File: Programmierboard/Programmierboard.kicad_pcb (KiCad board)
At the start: 2 copper layers, 179 x 99 mm, 37 parts, among them J1 Conn_01x10_Socket, J2 Conn_01x10_Socket, J3 Conn_01x10_Socket, J4 Conn_01x10_Socket, J5 DE9_Plug_MountingHoles, J6 Conn_01x10_Socket, J7 Conn_01x10_Socket, Q1 BC327, Q2 BC327, SW1 SW_SPDT, U1 AT89C2051-12P, U2 MAX202, U99 L7805

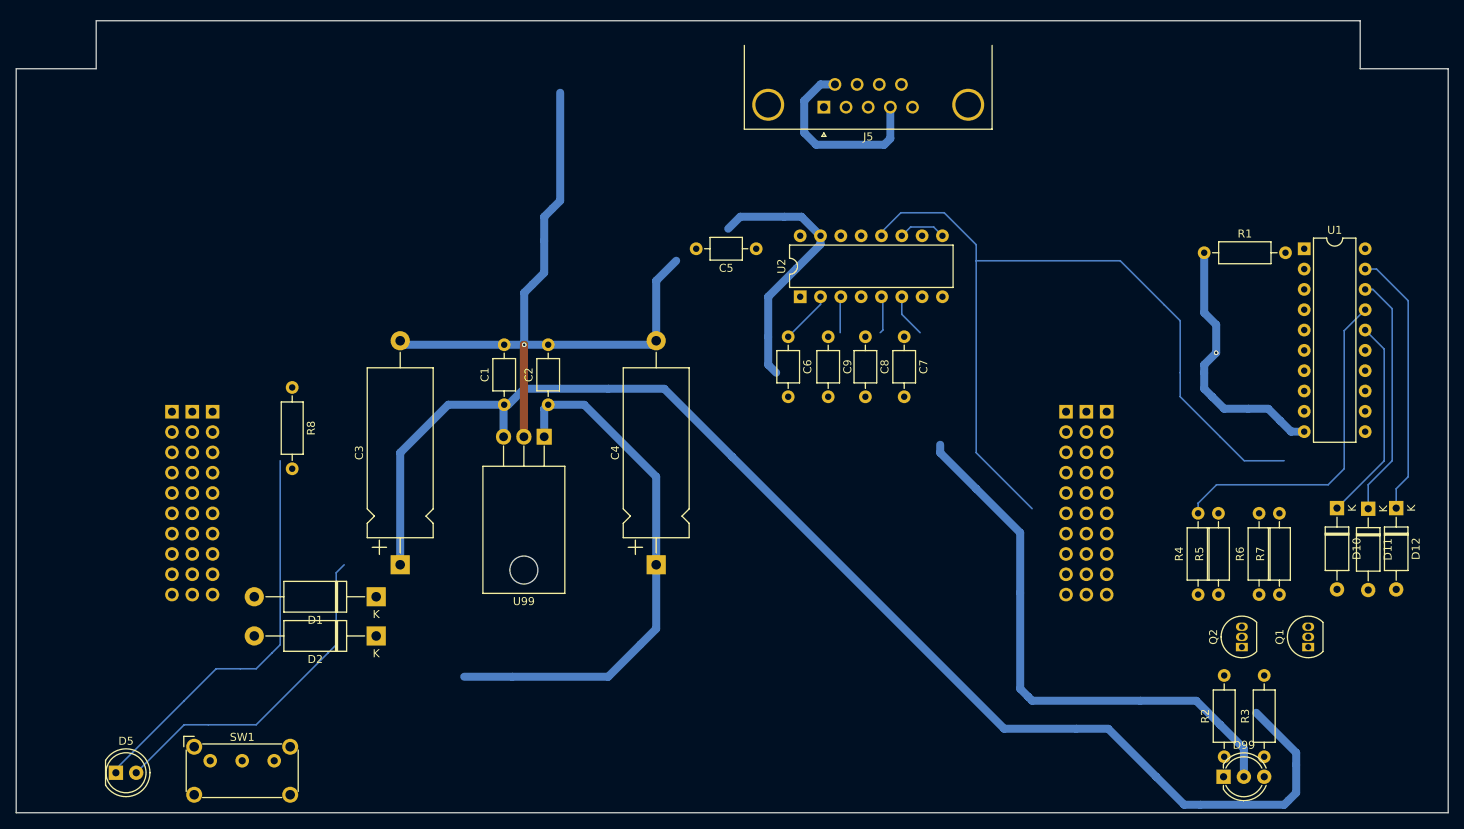
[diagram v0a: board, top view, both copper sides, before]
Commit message: footprints und symbole
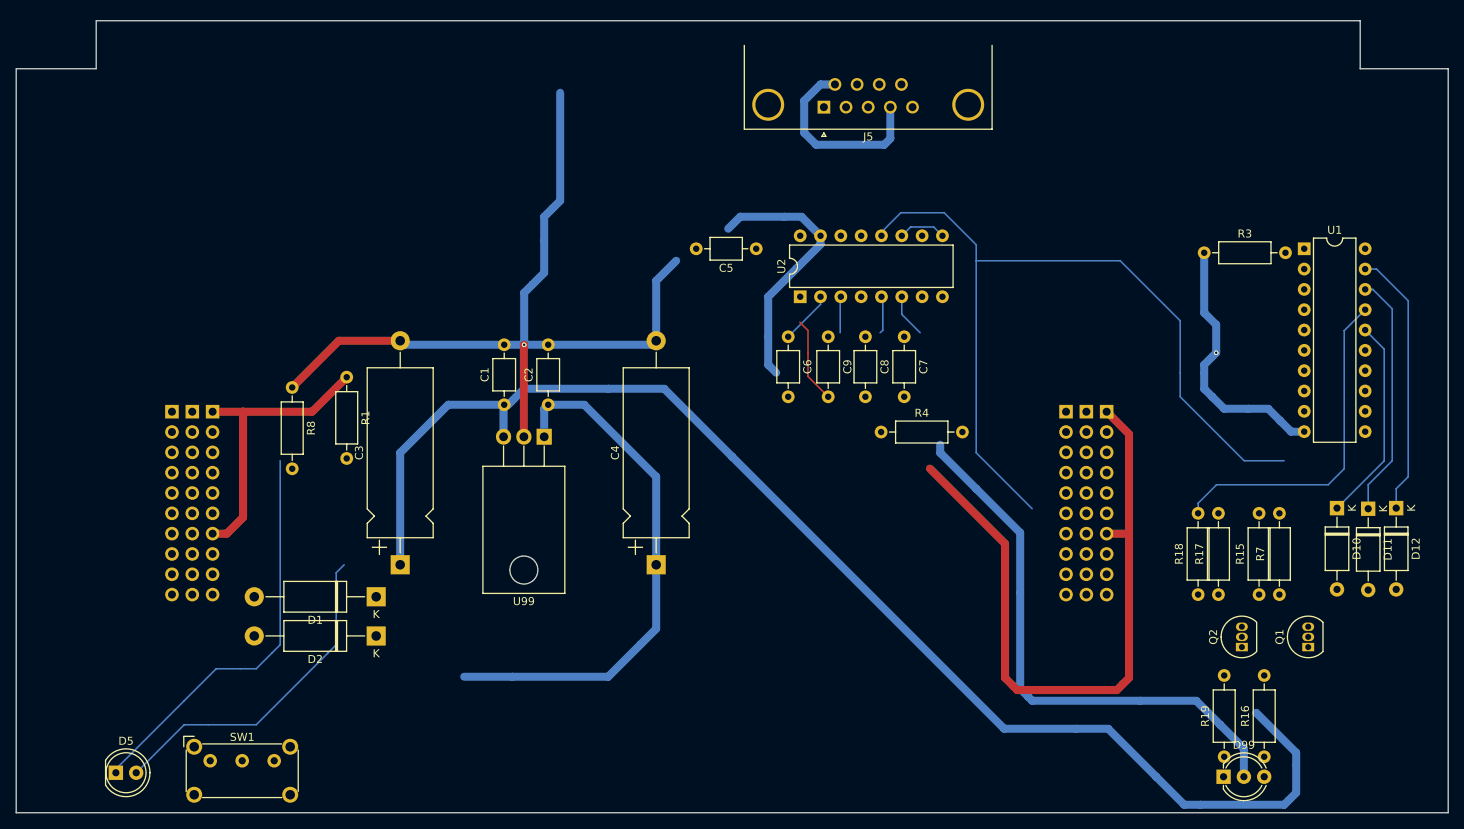
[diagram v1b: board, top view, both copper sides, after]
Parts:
- added R1: R, Resistor_THT:R_Axial_DIN0207_L6.3mm_D2.5mm_P10.16mm_Horizontal, F.Cu at (99.3, 98.6)
- added R4: R, Resistor_THT:R_Axial_DIN0207_L6.3mm_D2.5mm_P10.16mm_Horizontal, F.Cu at (166.1, 105.4)
- renumbered R6 to R15, R3 to R16, R5 to R17, R4 to R18, R2 to R19, R1 to R3
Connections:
- J1 pad 1: unconnected-(J1-Pin_1-Pad1) -> Net-(J1-Pin_1)
- J1 pad 7: unconnected-(J1-Pin_7-Pad7) -> Net-(J1-Pin_1)
- J4 pad 1: unconnected-(J4-Pin_1-Pad1) -> Net-(J4-Pin_1)
- J4 pad 7: unconnected-(J4-Pin_7-Pad7) -> Net-(J4-Pin_1)
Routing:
- net Net-(J1-Pin_1): track 0.00 -> 84.0 mm
- net Net-(J4-Pin_1): track 0.00 -> 36.4 mm
- net GND: track 223.9 -> 239.8 mm
- net unconnected-(C9-Pad2): track 0.00 -> 10.8 mm

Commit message: prog
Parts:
- added C10: C, Capacitor_THT:C_Axial_L3.8mm_D2.6mm_P7.50mm_Horizontal, F.Cu at (221.4, 79.4)
- added J8: Conn_01x02_Socket, Connector_PinSocket_2.54mm:PinSocket_1x02_P2.54mm_Vertical, F.Cu at (119.5, 82.5)
- D5: value LED -> POWER
- moved Q2 4.89 mm to (206.4, 131.6)
- moved Q1 4.78 mm to (214.8, 131.7)
- moved R19 3.58 mm to (205.7, 144.5)
- moved R16 3.34 mm to (211.1, 144.4)
- moved D99 2.94 mm to (206.0, 148.2)
- moved U2 1.87 mm to (154.3, 89.3)
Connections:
- C1 pad 1: Net-(U99-OUT) -> VCC
- C3 pad 1: Net-(U99-OUT) -> VCC
- C5 pad 1: unconnected-(C5-Pad1) -> Net-(J1-Pin_1)
- C6 pad 2: unconnected-(C6-Pad2) -> GND
- C7 pad 2: unconnected-(C7-Pad2) -> GND
- D5 pad 2: unconnected-(D5-A-Pad2) -> VCC
- J4 pad 1: Net-(J4-Pin_1) -> Net-(J1-Pin_1)
- J4 pad 7: Net-(J4-Pin_1) -> Net-(J1-Pin_1)
- R1 pad 1: Net-(J4-Pin_1) -> Net-(J1-Pin_1)
- R1 pad 2: unconnected-(R1-Pad2) -> VCC
- R15 pad 2: Net-(R15-Pad2) -> VCC
- R17 pad 2: Net-(R15-Pad2) -> VCC
- U1 pad 20: unconnected-(U1-VCC-Pad20) -> VCC
- U99 pad 3: Net-(U99-OUT) -> VCC
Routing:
- net VCC: track 0.00 -> 251.6 mm
- net GND: track 239.8 -> 418.7 mm
- net Net-(U99-OUT): track 167.6 -> 0.00 mm
- net Net-(J1-Pin_1): track 84.0 -> 217.4 mm
- net +12V: track 0.00 -> 81.3 mm
- net unconnected-(D5-A-Pad2): track 42.0 -> 0.00 mm
- net Net-(J4-Pin_1): track 36.4 -> 0.00 mm
- net Net-(D1-K): track 66.9 -> 82.1 mm
- net unconnected-(U2-R1OUT-Pad12): track 105.3 -> 107.0 mm
- net Net-(U2-VS+): track 5.97 -> 4.48 mm

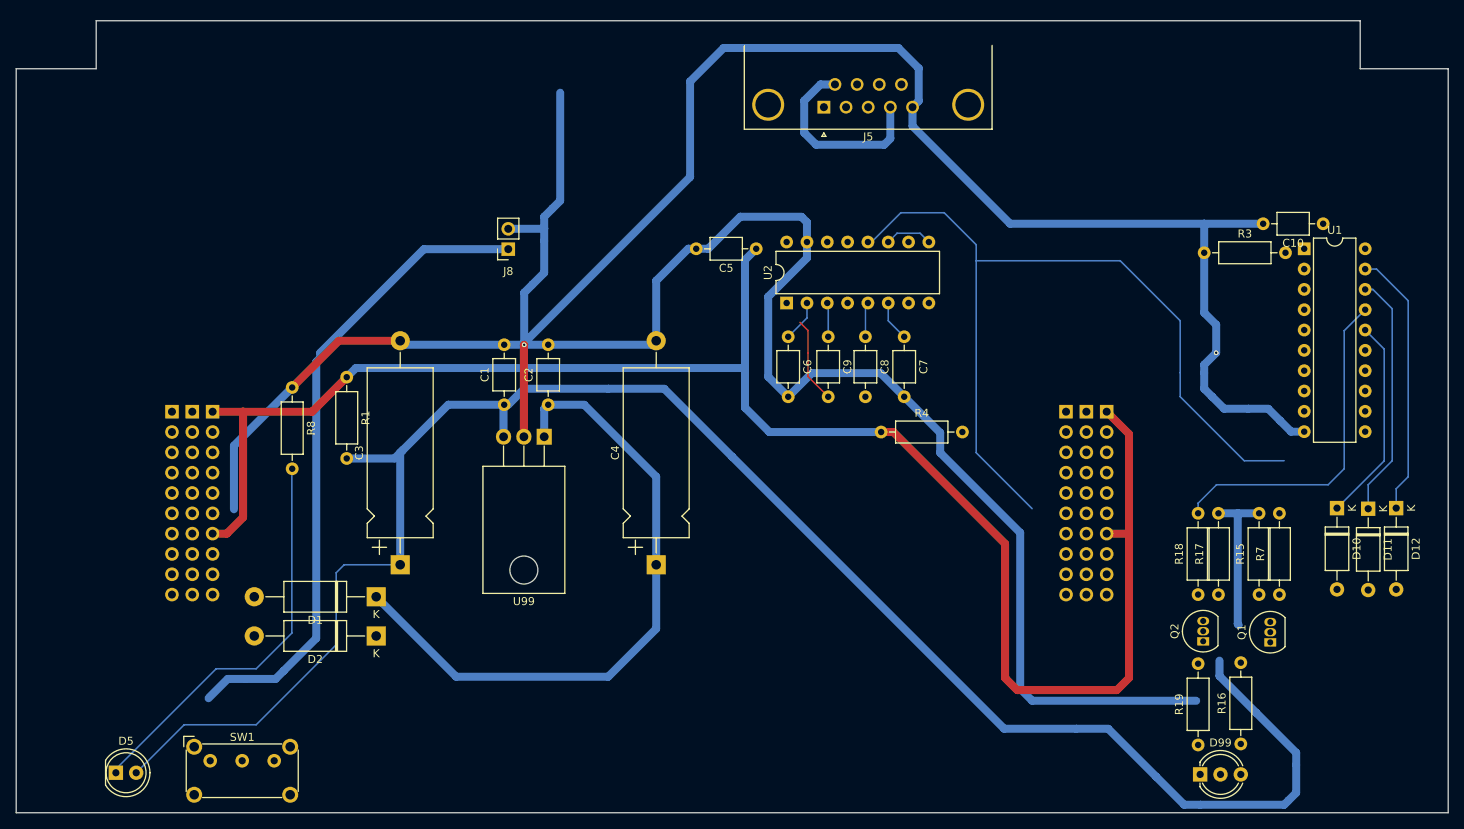
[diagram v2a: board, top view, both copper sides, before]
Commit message: programmierboard bis auf 2 linien
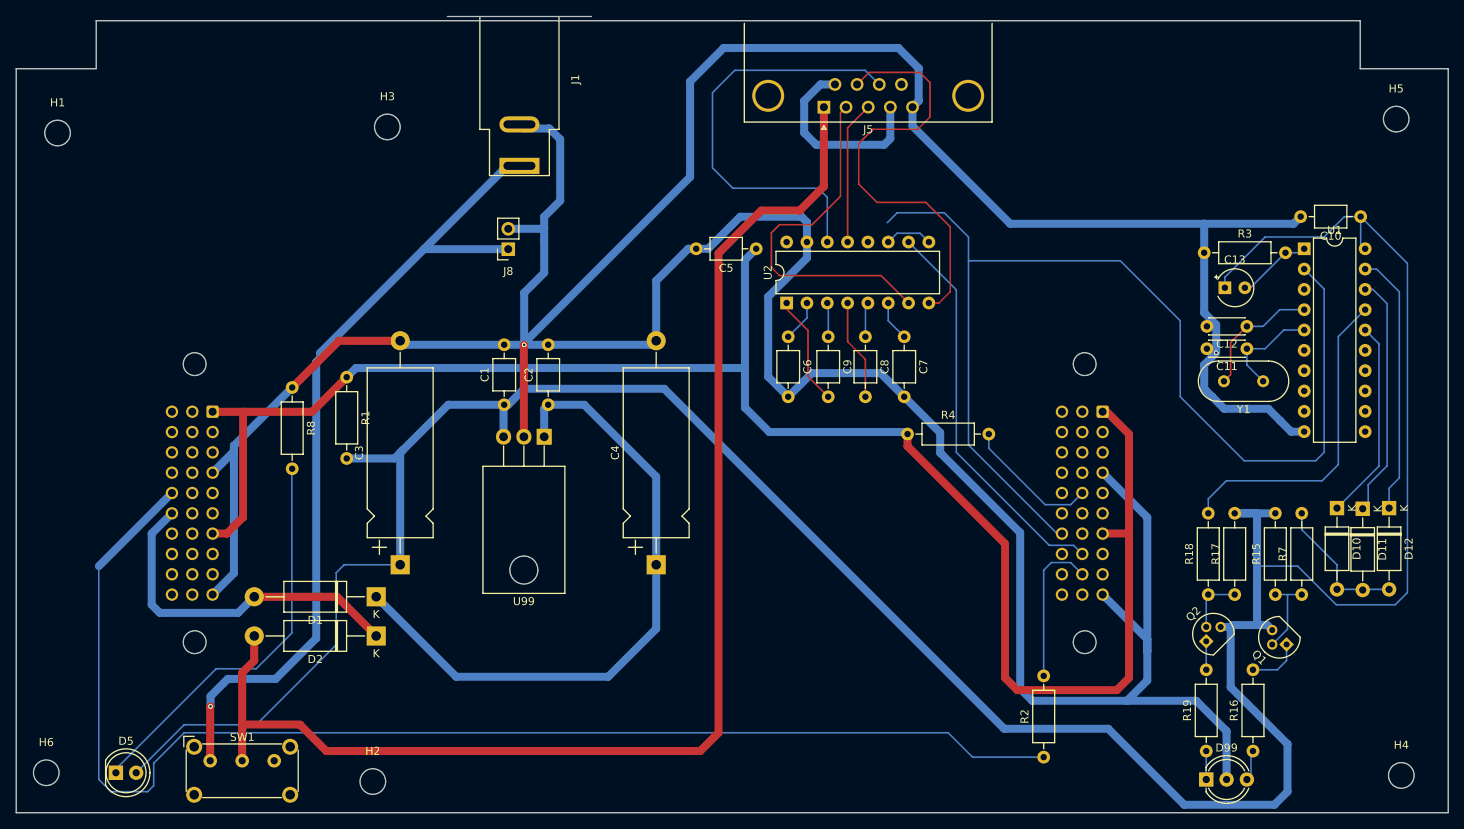
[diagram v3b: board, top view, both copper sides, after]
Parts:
- removed J2, J3, J4, J6, J7: Conn_01x10_Socket, Connector_PinSocket_2.54mm:PinSocket_1x10_P2.54mm_Vertical
- added C11: C, Capacitor_THT:C_Disc_D4.3mm_W1.9mm_P5.00mm, F.Cu at (211.8, 95.0)
- added C12: C, Capacitor_THT:C_Disc_D4.3mm_W1.9mm_P5.00mm, F.Cu at (211.8, 92.2)
- added C13: C, Capacitor_THT:CP_Radial_Tantal_D4.5mm_P2.50mm, F.Cu at (209.1, 87.4)
- added H1: MountingHole, MountingHole:MountingHole_3.2mm_M3_DIN965, F.Cu at (63.2, 68.0)
- added H2: MountingHole, MountingHole:MountingHole_3.2mm_M3_DIN965, F.Cu at (102.6, 149.1)
- added H3: MountingHole, MountingHole:MountingHole_3.2mm_M3_DIN965, F.Cu at (104.4, 67.3)
- added H4: MountingHole, MountingHole:MountingHole_3.2mm_M3_DIN965, F.Cu at (231.1, 148.3)
- added H5: MountingHole, MountingHole:MountingHole_3.2mm_M3_DIN965, F.Cu at (230.5, 66.3)
- added H6: MountingHole, MountingHole:MountingHole_3.2mm_M3_DIN965, F.Cu at (61.8, 148.0)
- added J10: DIN41612_03x10_ABC, Connector_DIN:DIN41612_C3_3x10_Female_Vertical_THT, B.Cu at (193.8, 102.9)
- added J9: DIN41612_03x10_ABC, Connector_DIN:DIN41612_C3_3x10_Female_Vertical_THT, B.Cu at (82.5, 102.9)
- added R2: 1, Resistor_THT:R_Axial_DIN0207_L6.3mm_D2.5mm_P10.16mm_Horizontal, F.Cu at (186.4, 146.1)
- added Y1: Crystal, Crystal:Crystal_HC18-U_Vertical, F.Cu at (213.9, 99.1)
- J1: value Conn_01x10_Socket -> Barrel_Jack; footprint Connector_PinSocket_2.54mm:PinSocket_1x10_P2.54mm_Vertical -> Connector_BarrelJack:BarrelJack_SwitchcraftConxall_RAPC10U_Horizontal; moved to F.Cu
- J5: footprint Connector_Dsub:DSUB-9_Female_Horizontal_P2.77x2.84mm_EdgePinOffset4.94mm_Housed_MountingHolesOffset7.48mm -> Connector_Dsub:DSUB-9_Socket_Horizontal_P2.77x2.84mm_EdgePinOffset7.70mm_Housed_MountingHolesOffset9.12mm
- Q1, Q2: footprint Package_TO_SOT_THT:TO-92_Inline -> Package_TO_SOT_THT:TO-92
- R1, R4: value R -> 1
- R16, R19: value R -> 120
- moved J1 79.6 mm to (120.9, 72.1), turned to -90 degrees
- moved C10 4.78 mm to (226.1, 78.5)
- moved R4 3.31 mm to (169.4, 105.7)
- moved R7 2.79 mm to (218.7, 125.7)
- moved Q1 2.06 mm to (216.8, 132.0), turned to 135 degrees
- moved R17 2.03 mm to (210.3, 125.7)
- moved R15 2.03 mm to (215.4, 125.7)
- moved R16 1.76 mm to (212.6, 145.3)
- moved R19 1.27 mm to (206.8, 145.3)
- moved R18 1.27 mm to (207.0, 125.7)
- moved D99 0.99 mm to (206.8, 148.8)
- moved D12 0.88 mm to (229.6, 114.9)
- moved D11 0.69 mm to (226.3, 115.0)
- moved Q2 0.38 mm to (206.8, 131.6), turned to 45 degrees
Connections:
- C5 pad 1: Net-(J1-Pin_1) -> Net-(J10A-Pin_a1)
- C8 pad 2: unconnected-(C8-Pad2) -> Net-(U2-C2+)
- C9 pad 2: unconnected-(C9-Pad2) -> Net-(U2-C1+)
- D1 pad 2: unconnected-(D1-A-Pad2) -> Net-(D1-A)
- D10 pad 2: unconnected-(D10-A-Pad2) -> Net-(D10-A)
- D11 pad 2: unconnected-(D11-A-Pad2) -> Net-(D10-A)
- D12 pad 2: unconnected-(D12-A-Pad2) -> Net-(D10-A)
- D2 pad 1: unconnected-(D2-K-Pad1) -> Net-(D1-A)
- D2 pad 2: unconnected-(D2-A-Pad2) -> Net-(D2-A)
- J1 pad 1: Net-(J1-Pin_1) -> Net-(J8-Pin_1)
- J1 pad 2: unconnected-(J1-Pin_2-Pad2) -> GND
- J5 pad 1: unconnected-(J5-Pad1) -> Net-(D2-A)
- J5 pad 2: unconnected-(J5-Pad2) -> Net-(U2-T2OUT)
- J5 pad 3: unconnected-(J5-Pad3) -> Net-(U2-R1IN)
- J5 pad 7: unconnected-(J5-Pad7) -> Net-(U2-R2IN)
- J8 pad 1: +12V -> Net-(J8-Pin_1)
- Q1 pad 1: unconnected-(Q1-C-Pad1) -> Net-(Q1-C)
- Q1 pad 2: unconnected-(Q1-B-Pad2) -> Net-(Q1-B)
- Q1 pad 3: unconnected-(Q1-E-Pad3) -> VCC
- Q2 pad 1: unconnected-(Q2-C-Pad1) -> Net-(Q2-C)
- Q2 pad 2: unconnected-(Q2-B-Pad2) -> Net-(Q2-B)
- Q2 pad 3: unconnected-(Q2-E-Pad3) -> VCC
- R1 pad 1: Net-(J1-Pin_1) -> Net-(J10A-Pin_a1)
- R15 pad 1: unconnected-(R15-Pad1) -> Net-(Q1-B)
- R16 pad 2: unconnected-(R16-Pad2) -> Net-(Q1-C)
- R17 pad 1: unconnected-(R17-Pad1) -> Net-(Q2-B)
- R18 pad 1: unconnected-(R18-Pad1) -> Net-(Q2-B)
- R19 pad 2: unconnected-(R19-Pad2) -> Net-(Q2-C)
- R3 pad 2: unconnected-(R3-Pad2) -> Net-(U1-RST/VPP)
- R4 pad 1: Net-(J1-Pin_1) -> Net-(J10A-Pin_a1)
- R4 pad 2: unconnected-(R4-Pad2) -> Net-(J10B-Pin_b5)
- R7 pad 1: unconnected-(R7-Pad1) -> Net-(Q1-B)
- R7 pad 2: unconnected-(R7-Pad2) -> Net-(D10-A)
- SW1 pad 1: unconnected-(SW1-A-Pad1) -> Net-(J8-Pin_1)
- SW1 pad 2: unconnected-(SW1-B-Pad2) -> Net-(D2-A)
- U1 pad 1: unconnected-(U1-RST/VPP-Pad1) -> Net-(U1-RST/VPP)
- U1 pad 2: unconnected-(U1-P3.0-Pad2) -> Net-(J10C-Pin_c7)
- U1 pad 4: unconnected-(U1-XTAL2-Pad4) -> Net-(U1-XTAL2)
- U1 pad 5: unconnected-(U1-XTAL1-Pad5) -> Net-(U1-XTAL1)
- U2 pad 1: unconnected-(U2-C1+-Pad1) -> Net-(U2-C1+)
- U2 pad 10: unconnected-(U2-T2IN-Pad10) -> Net-(J10B-Pin_b8)
- U2 pad 13: unconnected-(U2-R1IN-Pad13) -> Net-(U2-R1IN)
- U2 pad 4: unconnected-(U2-C2+-Pad4) -> Net-(U2-C2+)
- U2 pad 7: unconnected-(U2-T2OUT-Pad7) -> Net-(U2-T2OUT)
- U2 pad 8: unconnected-(U2-R2IN-Pad8) -> Net-(U2-R2IN)
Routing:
- net Net-(J10A-Pin_a1): track 0.00 -> 218.3 mm
- net Net-(J1-Pin_1): track 217.4 -> 0.00 mm
- net Net-(D2-A): track 0.00 -> 164.6 mm
- net Net-(J9C-Pin_c5): track 0.00 -> 164.3 mm
- net Net-(J10C-Pin_c7): track 0.00 -> 139.0 mm
- net VCC: track 251.6 -> 359.7 mm
- net unconnected-(U2-R1OUT-Pad12): track 107.0 -> 0.45 mm
- net Net-(J8-Pin_1): track 0.00 -> 105.3 mm, vias 0 -> 1
- net +12V: track 81.3 -> 0.00 mm
- net GND: track 418.7 -> 492.8 mm
- net Net-(U2-R2IN): track 0.00 -> 54.9 mm
- net Net-(U2-T1OUT): track 0.00 -> 53.6 mm
- net Net-(J10B-Pin_b8): track 0.00 -> 49.8 mm
- net Net-(U2-T2OUT): track 0.00 -> 45.3 mm
- net Net-(D1-A): track 0.00 -> 43.8 mm
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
